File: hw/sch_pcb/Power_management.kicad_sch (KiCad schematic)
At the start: 47 parts, among them IC3 LTC4041EUFD#PBF, J19 Conn_01x03_Male, J20 Conn_01x03_Male, J24 HEADER_2x03_PARALLEL, J5 HEADER_2x03_PARALLEL, Q2 SIR424DP, Q3 SIR424DP, U10 TPS631000DRLR, U8 MIC5504-1.8YM5-TR, U9 TPS631000DRLR

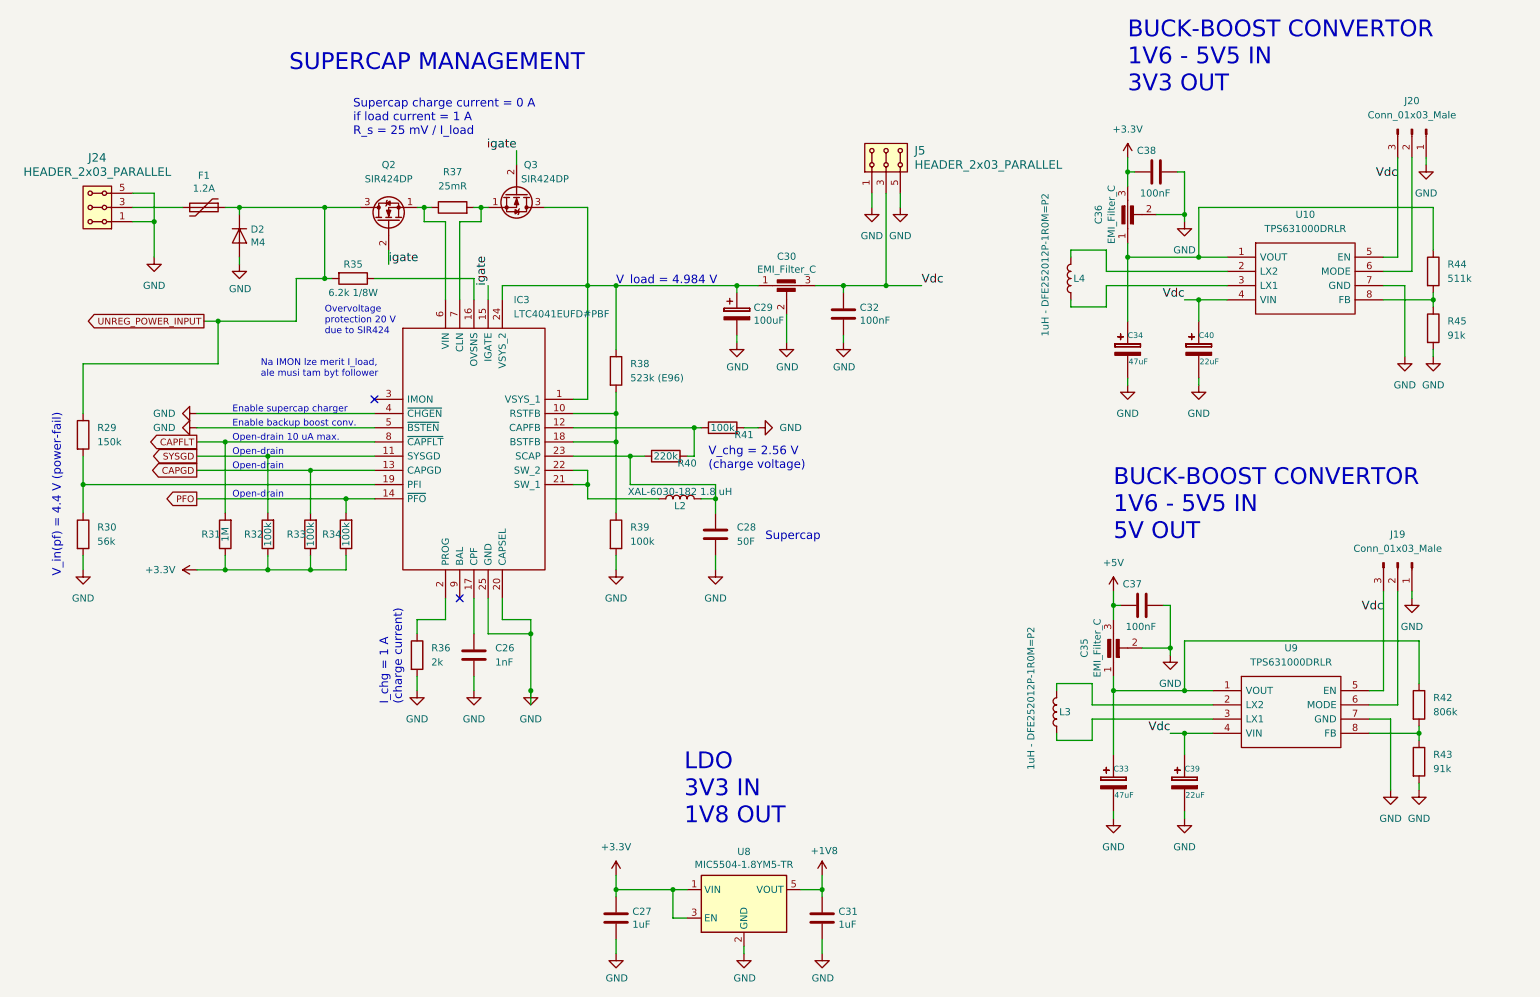
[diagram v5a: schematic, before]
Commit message: Update footprints. Improve layout Fix some DRC errors. Set components values matching inventory.
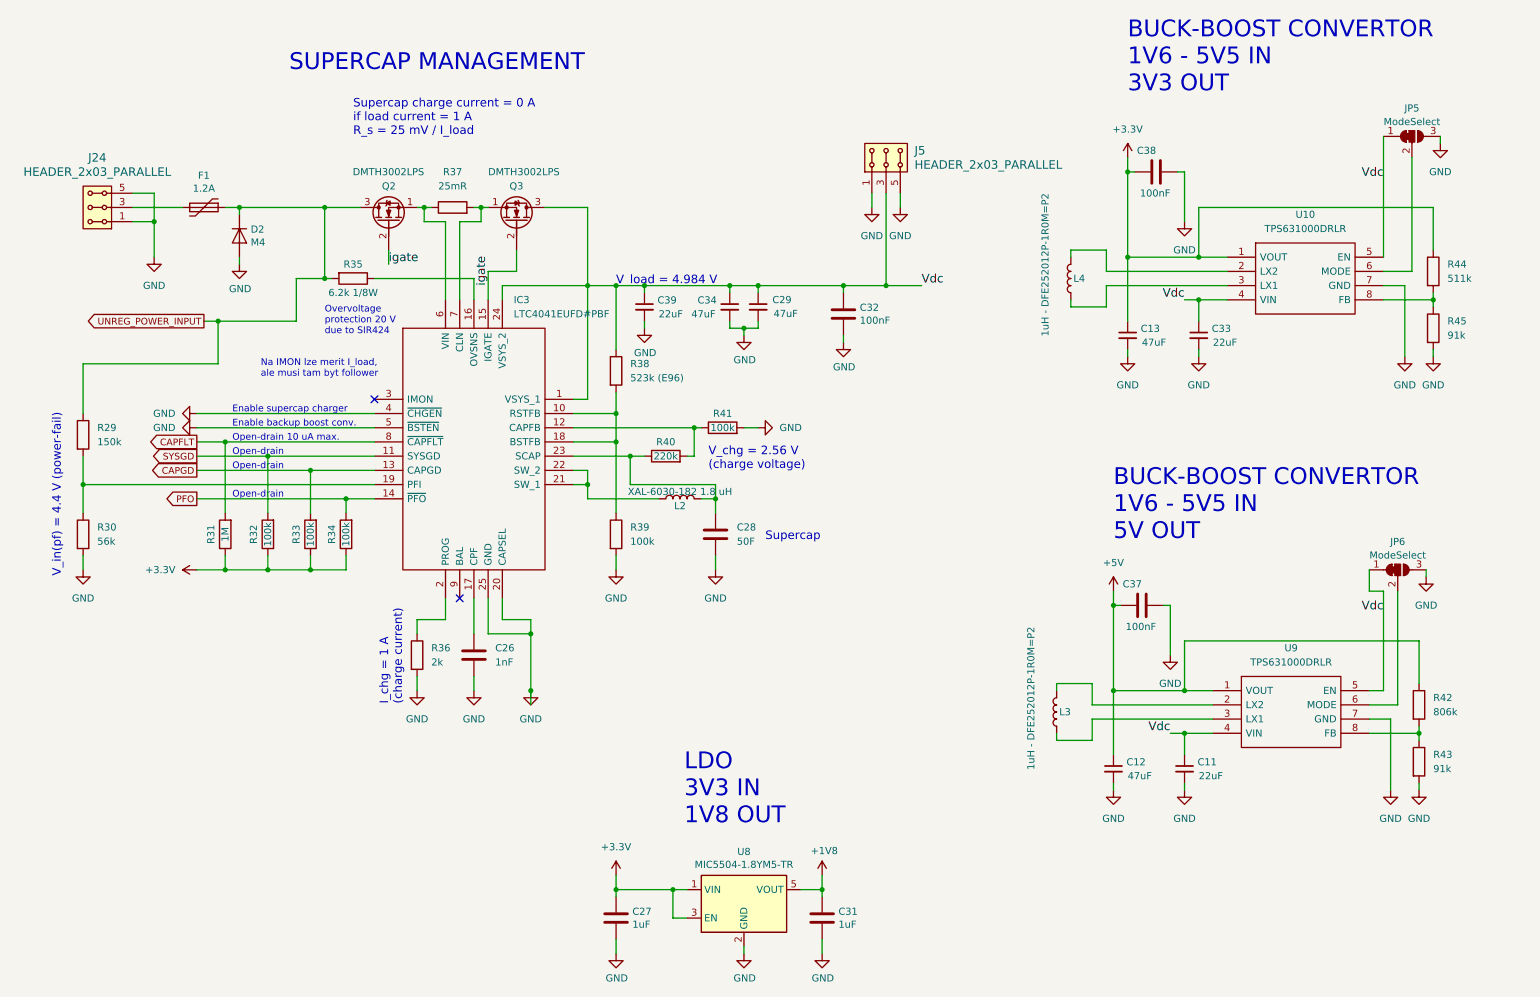
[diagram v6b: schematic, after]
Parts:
- removed C29: 100uF, Mlab_C:TantalC_SizeC_Reflow, symbol DATALOGGER01A-rescue:CP-device
- removed C30, C35, C36: EMI_Filter_C, Mlab_L:FIR_0805, symbol DATALOGGER01A-rescue:EMI_Filter_C-device
- removed C33, C34: 47uF, Mlab_C:TantalC_SizeB_Reflow, symbol LION2CELL01D-rescue:CP2
- removed C39, C40: 22uF, Mlab_C:TantalC_SizeB_Reflow, symbol LION2CELL01D-rescue:CP2
- removed J19, J20: Conn_01x03_Male, Mlab_Pin_Headers:Straight_1x03, symbol Connector:Conn_01x03_Male
- removed Q2, Q3: SIR424DP, Package_TO_SOT_THT:TO-92_Inline, symbol Transistor_FET:2N7000
- added C11, C33, C39: 22uF, Capacitor_SMD:C_0805_2012Metric, symbol Device:C_Small
- added C12, C13, C29, C34: 47uF, Capacitor_SMD:C_0805_2012Metric, symbol Device:C_Small
- added JP5, JP6: ModeSelect, Jumper:SolderJumper-3_P1.3mm_Bridged12_RoundedPad1.0x1.5mm_NumberLabels, symbol Jumper:SolderJumper_3_Bridged12
- added Q2, Q3: DMTH3002LPS, Mlab_T:D_POWERDI5060-8_6.0x5.1mm_P1.27mm, symbol Device:Q_NMOS_SGD
- C26, C27, C31, C32, C37, C38: footprint Mlab_C:SMD-0805 -> Capacitor_SMD:C_0805_2012Metric
- C28: footprint Mlab_C:C_Radial_D16_L25_P7.5 -> Capacitor_THT:CP_Radial_D18.0mm_P7.50mm
- R29, R30, R31, R32, R33, R34, R35, R36, R37, R38, R39, R40, R41, R42, R43, R44, R45: footprint Mlab_R:SMD-0805 -> Resistor_SMD:R_0805_2012Metric
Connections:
- net +3.3V: now also R44.1, U10.1 (VOUT), C13.1
- net +5V: now also R42.1, U9.1 (VOUT), C12.1
- net GND: now also C11.2, C12.2, C13.2, C29.2, C33.2, C34.2, C39.2, JP5.3 (B), JP6.3 (B)
- net UNREG_POWER_INPUT: now also Q2.3 (D)
- net Vdc: now also IC3.1 (VSYS_1), IC3.24 (VSYS_2), R38.1, C11.1, C29.1, C33.1, C34.1, C39.1, JP5.1 (A), JP6.1 (A), Q3.3 (D)
- net igate: now also Q2.2 (G), Q3.2 (G)
- net at IC3.6 (VIN), R37.1: now also Q2.1 (S)
- net at IC3.7 (CLN), R37.2: now also Q3.1 (S)
- net at U9.6 (MODE): now also JP6.2 (C)
- net at U10.6 (MODE): now also JP5.2 (C)
